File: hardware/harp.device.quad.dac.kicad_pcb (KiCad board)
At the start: 4 copper layers, 90 x 100 mm, 261 parts, among them J1 5-146281-3, J10 Conn_Coaxial, J11 Conn_Coaxial, J12 Conn_Coaxial, J13 Conn_Coaxial, J14 Barrel_Jack_Switch, J15 Conn_Coaxial, J16 Conn_Coaxial, J17 Conn_Coaxial, J18 Conn_Coaxial, J2 5-146281-3, J3 AudioJack3, J4 USB_C_Receptacle_USB2.0, J5 Micro_SD_Card_Det_Hirose_DM3AT, J6 Conn_Coaxial, J7 Conn_Coaxial, J8 Conn_Coaxial, J9 Conn_Coaxial, Q1 Si2369DS, Q2 Si2369DS, Q3 Si2369DS, SW1 SPST-NO, SW2 SPST-NO, U1 LM337_SOT223, U10 LTC2642, U11 LTC2642, U12 REF35250QDBVR, U13 LMV393IDGKR, U14 LMV393IDGKR, U15 LMV393IDGKR, U16 LMV393IDGKR, U17 INA181, U18 INA181, U19 INA181, U2 W25Q16JVUXIQ, U20 INA181, U21 REF2033, U22 SN74LVC2T45DCTR, U23 SN74LVC2T45DCTR, U24 rt6150b-33gqw, U25 TPS65131RGE, U27 LM2940IMPX-12/NOPB, U29 LMR51430, U3 ADUM4160, U30 SN74LVC2T45DCTR, U31 SN74LVC2T45DCTR, U32 RP2350_80QFN, U4 OPA2994IDGKR, U5 OPA2994IDGKR, U6 OPA2994IDGKR, U7 OPA2994IDGKR, U8 LTC2642, U9 LTC2642

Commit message: update pcb
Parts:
- removed C3: 10uF, Capacitor_SMD:C_0603_1608Metric
- removed SW1: SPST-NO, kicad-lib:SW_Push_1P1T-SH_NO_Vertical_Wuerth_WS-TASV
- added R19: 10K, Resistor_SMD:R_0402_1005Metric, F.Cu at (127.1, 81.7)
- added R22: 10K, Resistor_SMD:R_0402_1005Metric, F.Cu at (127.1, 63.7)
- R1: value 100 -> 10K; footprint Resistor_SMD:R_0603_1608Metric -> Resistor_SMD:R_0402_1005Metric
- moved C15 66.2 mm to (141.6, 97.2)
- moved R1 65.4 mm to (127.1, 117.7)
- moved R4 49.9 mm to (127.1, 99.6)
- moved C14 5.01 mm to (87.4, 64.7)
- moved J1 0.50 mm to (144.3, 99.7)
- moved D2 0.45 mm to (147.2, 97.2)
- moved D1 0.40 mm to (144.6, 97.2)
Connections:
- R1 pad 1: Net-(R1-Pad1) -> DAC_3_CS
- R1 pad 2: Net-(U32-RUN) -> +3.3V
- R4 pad 1: +3.3V -> DAC_2_CS
- R4 pad 2: Net-(U32-RUN) -> +3.3V
- U32 pad 35: Net-(U32-RUN) -> +3.3V
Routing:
- net /RP2350 Core/HARP_CLK_SYNC: track 19.0 -> 57.2 mm, vias 3 -> 4
- net DAC_2_CS: track 18.6 -> 22.1 mm
- net DAC_1_CS: track 10.8 -> 14.1 mm
- net DAC_0_CS: track 25.7 -> 29.0 mm
- net DAC_3_CS: track 32.9 -> 36.2 mm
- net +3.3V: track 215.5 -> 218.7 mm, vias 74 -> 79
- net GND: track 119.6 -> 120.7 mm, vias 159 -> 160
- net SHORT_CIRCUIT_3: track 44.6 -> 45.4 mm
- net /RP2350 Core/USB-: track 0.00 -> 0.67 mm, vias 0 -> 1
- net /RP2350 Core/USB+: track 0.00 -> 0.67 mm, vias 0 -> 1
- net SHORT_CIRCUIT_2: track 30.8 -> 31.4 mm

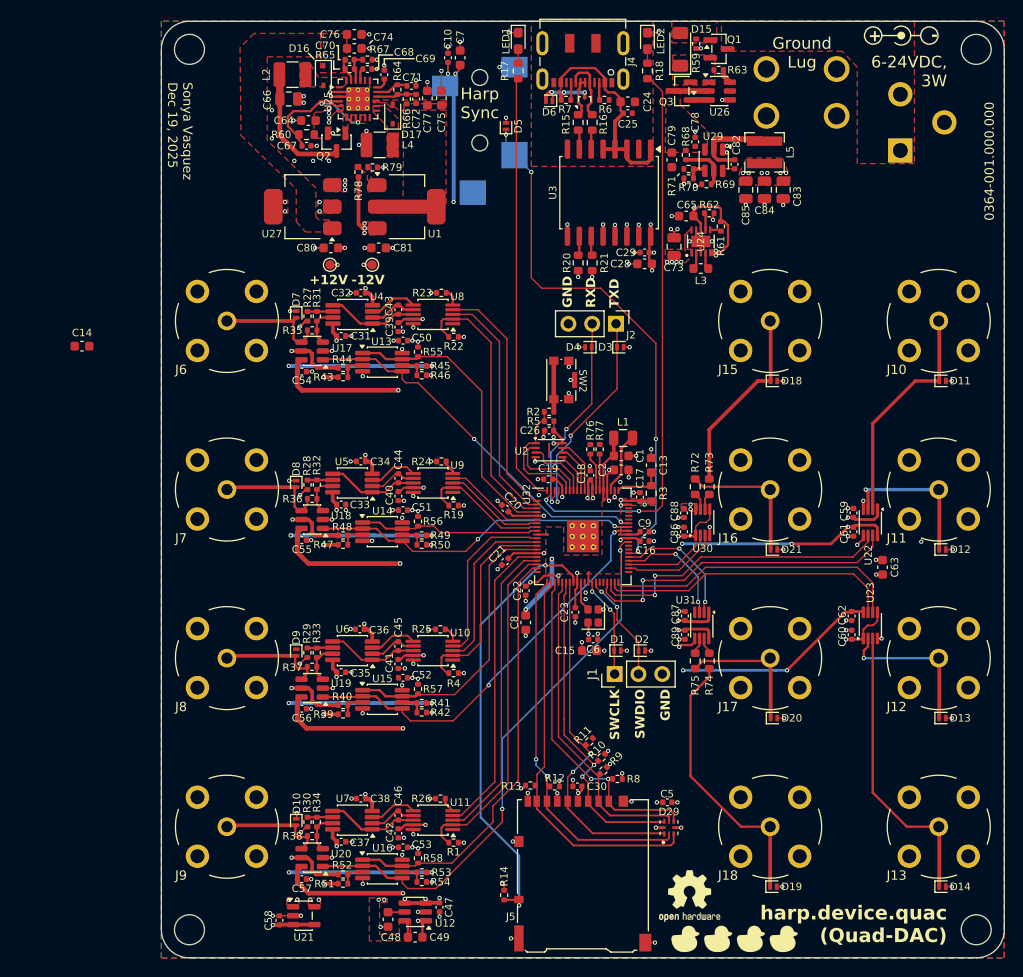
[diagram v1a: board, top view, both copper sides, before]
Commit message: fix sd card order; finish pcb draft
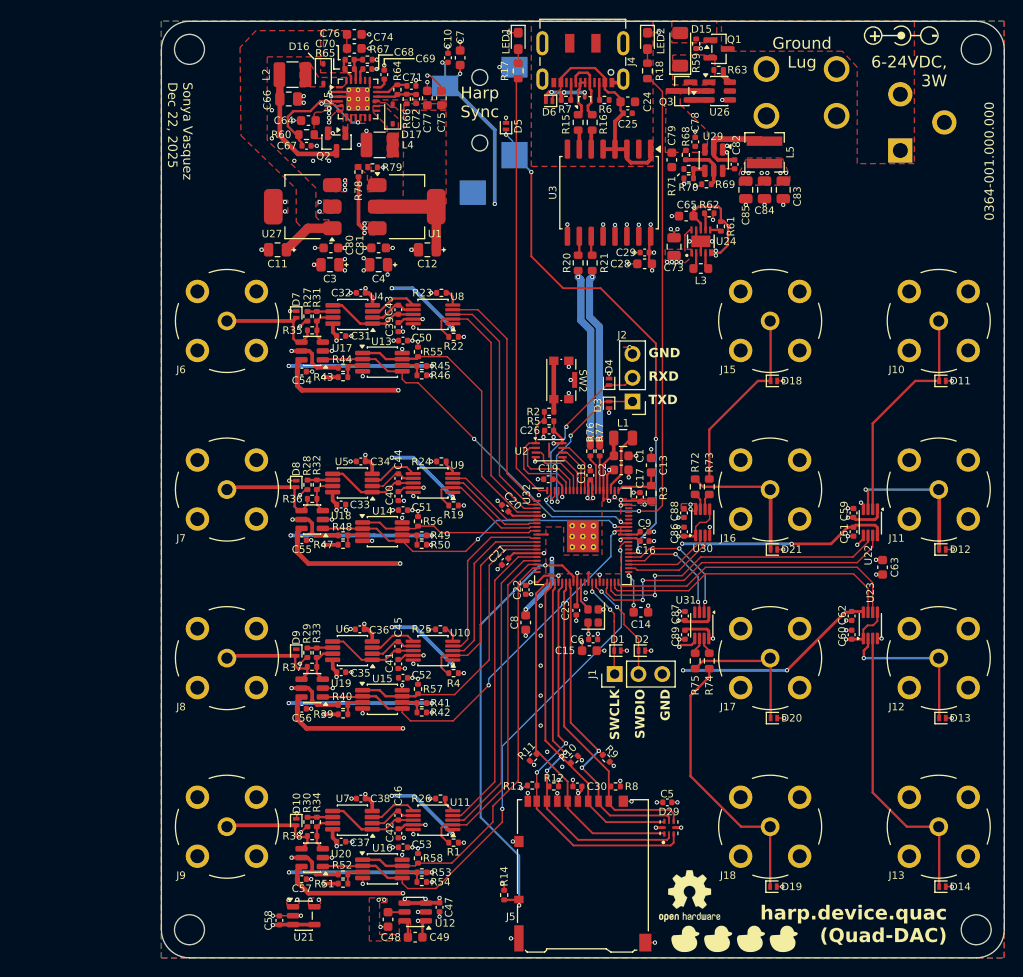
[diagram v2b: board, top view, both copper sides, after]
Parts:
- removed TP1, TP2: TestPoint, TestPoint:TestPoint_Pad_D1.0mm
- added C11: 1uF, kicad-lib:C_Polarized_0805_2012Metric, F.Cu at (108.3, 54.4)
- added C12: 1uF, kicad-lib:C_Polarized_0805_2012Metric, F.Cu at (124.3, 54.4)
- added C3: 1uF, kicad-lib:C_Polarized_0805_2012Metric, F.Cu at (113.9, 56.0)
- added C4: 1uF, kicad-lib:C_Polarized_0805_2012Metric, F.Cu at (119.1, 56.0)
- R65: value 1M -> 1M05
- R66: value 1M1 -> 1M15
- moved C14 66.1 mm to (147.1, 93.1)
- moved J2 8.48 mm to (146.2, 70.6), turned to 180 degrees
- moved D3 6.27 mm to (143.7, 71.0), turned to -90 degrees
- moved R11 6.24 mm to (135.6, 108.6), turned to 45 degrees
- moved D4 4.30 mm to (143.7, 68.5), turned to 90 degrees
- moved R10 2.91 mm to (140.0, 108.8)
- moved R9 1.33 mm to (143.4, 108.7), turned to 135 degrees
- moved R8 0.82 mm to (144.4, 111.7)
- moved C23 0.22 mm to (140.2, 92.9)
- moved R13 0.20 mm to (135.5, 111.6)
- moved R76 0.20 mm to (141.7, 75.9)
- moved R77 0.20 mm to (142.7, 75.9)
- moved D16 0.20 mm to (113.2, 35.6)
- moved C22 0.10 mm to (134.8, 90.7)
- moved R12 0.10 mm to (137.8, 111.7)
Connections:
- R58 pad 2: unconnected-(R58-Pad2) -> +3.3V
- U32 pad 21: /RP2350 Core/SD_DAT0 -> /RP2350 Core/SD_CLK
- U32 pad 22: /RP2350 Core/SD_DAT1 -> /RP2350 Core/SD_CMD
- U32 pad 23: /RP2350 Core/SD_DAT2 -> /RP2350 Core/SD_DAT0
- U32 pad 25: /RP2350 Core/SD_DAT3 -> /RP2350 Core/SD_DAT1
- U32 pad 26: /RP2350 Core/SD_CMD -> /RP2350 Core/SD_DAT2
- U32 pad 27: /RP2350 Core/SD_CLK -> /RP2350 Core/SD_DAT3
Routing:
- net VREF_2V5: track 1.90 -> 36.8 mm, vias 2 -> 10
- net /RP2350 Core/USB+: track 0.67 -> 19.3 mm, vias 1 -> 2
- net /RP2350 Core/USB-: track 0.67 -> 19.3 mm, vias 1 -> 2
- net +3.3V: track 218.7 -> 228.5 mm, vias 79 -> 82
- net /RP2350 Core/DEBUG_UART_TX: track 23.0 -> 17.1 mm
- net Net-(D16-K): track 2.64 -> 8.49 mm
- net Net-(D17-A): track 6.30 -> 10.9 mm
- net GND: track 120.7 -> 125.3 mm, vias 160 -> 173
- net /RP2350 Core/DEBUG_UART_RX: track 22.2 -> 19.4 mm
- net /RP2350 Core/HARP_CLK_SYNC: track 57.2 -> 55.0 mm
- net /RP2350 Core/SD_DAT2: track 36.0 -> 34.1 mm, vias 2 -> 0
- net GND_PC: track 6.44 -> 7.81 mm
- net /RP2350 Core/SD_DAT3: track 34.5 -> 35.6 mm, vias 0 -> 2
- net -12V: track 18.5 -> 19.5 mm, vias 9 -> 10
- net /RP2350 Core/SD_DAT1: track 42.3 -> 43.3 mm, vias 0 -> 2
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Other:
- board text added: "Sonya Vasquez Dec 22, 2025"
- board text removed: "+12V"
- board text removed: "-12V"
- board text removed: "Sonya Vasquez Dec 19, 2025"

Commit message: update bom
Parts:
- R17, R18: value 330 -> 1K; footprint Resistor_SMD:R_0603_1608Metric -> Resistor_SMD:R_0402_1005Metric
- U12: value REF35250QDBVR -> REF3525
- U17, U18, U19, U20: value INA181 -> INA181A1
- moved R17 13.8 mm to (147.8, 34.8), turned to -90 degrees
- moved R18 13.8 mm to (134.0, 34.8), turned to -90 degrees
- moved D5 3.61 mm to (132.9, 44.8), turned to -90 degrees
- moved J3 2.30 mm to (129.9, 36.2)
- moved C7 1.94 mm to (127.4, 32.0)
- moved C10 1.36 mm to (126.1, 32.6)
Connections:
- net /RP2350 Core/QSPI_CS0 renamed /RP2350 Core/QSPI_CS
- R17 pad 1: /RP2350 Core/DEBUG_LED_1 -> Net-(LED2-A)
- R17 pad 2: Net-(LED1-A) -> /RP2350 Core/DEBUG_LED_0
- R18 pad 1: /RP2350 Core/DEBUG_LED_0 -> Net-(LED1-A)
- R18 pad 2: Net-(LED2-A) -> /RP2350 Core/DEBUG_LED_1
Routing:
- net /RP2350 Core/HARP_CLK_SYNC: track 55.0 -> 58.5 mm
- net /RP2350 Core/DEBUG_LED_1: track 46.0 -> 46.8 mm
- net /RP2350 Core/DEBUG_LED_0: track 60.9 -> 61.6 mm
